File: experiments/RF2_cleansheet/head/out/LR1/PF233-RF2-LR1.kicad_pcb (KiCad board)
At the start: 2 copper layers, 150 x 150 mm, 94 parts

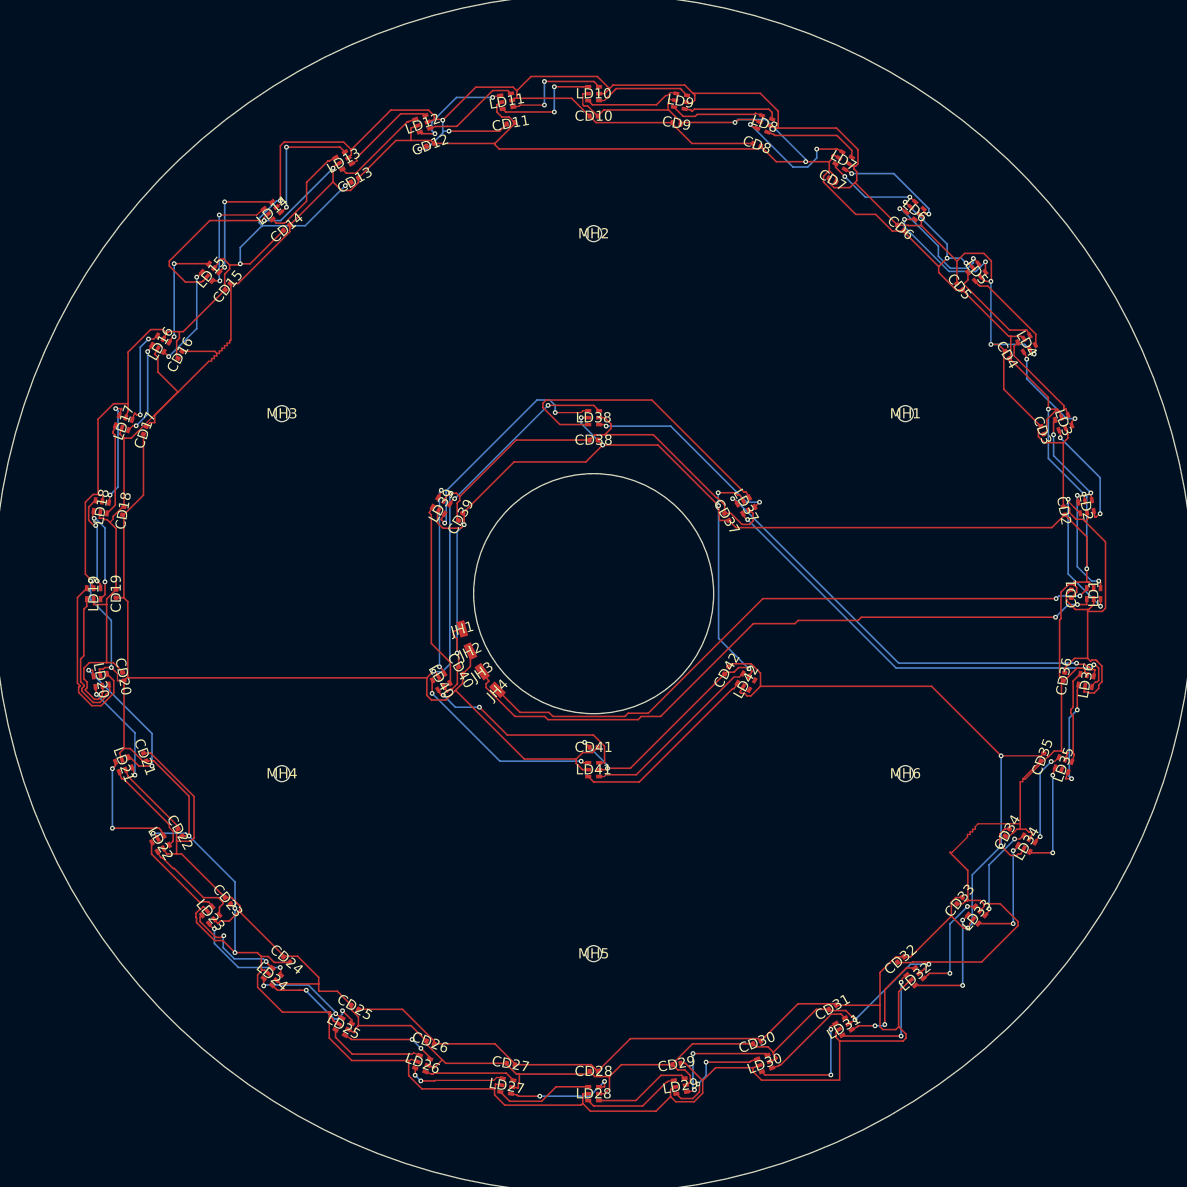
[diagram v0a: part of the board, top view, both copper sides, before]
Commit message: RF2: LED ring LR1 routed by a deterministic template (no autorouter), sign-off PASS
- rf2_ring_template.py: one cell per LED (data outer lane, clock inner lane, never crossing on a layer), chain links, power stubs to the open B.Cu buses, B.Cu crossings under the radial hinge feeds, and the 4 irregular links (hinge feeds, outer-to-inner jump). LR1: KiCad DRC 0, 0 unconnected, min clearance 0.19 mm (rule 0.10), no loop around the axis, parity, Gerbers; builds in 14 s. Freerouting had stalled (no pass in 5 min for 4 connections)
- netlist: LR1 capacitors rotated (+5V pin on the VDD side), hinge lands JH3 = clock / JH4 = data (harness C10c/C10d follow)
- rf2_boards: no autorouter run when nothing is open (template, pre-routes or resumed copper); board-setup via minima and a .kicad_dru written beside each board; freeroute --no-fanout for resumes
- rf2_head: LED envelope no longer empty (zero-height solid), capacitor sites added
- sign-off order: ledger before the housing checks. Head mass corrected 702 -> 745 g (docs/CORRECTIONS.md)
- Freerouting scratch folders untracked

Co-Authored-By: Claude Opus 5.5 <noreply@anthropic.com>
Claude-Session: https://claude.ai/code/session_01FX4DWSYYjMCFGGA6gmha65
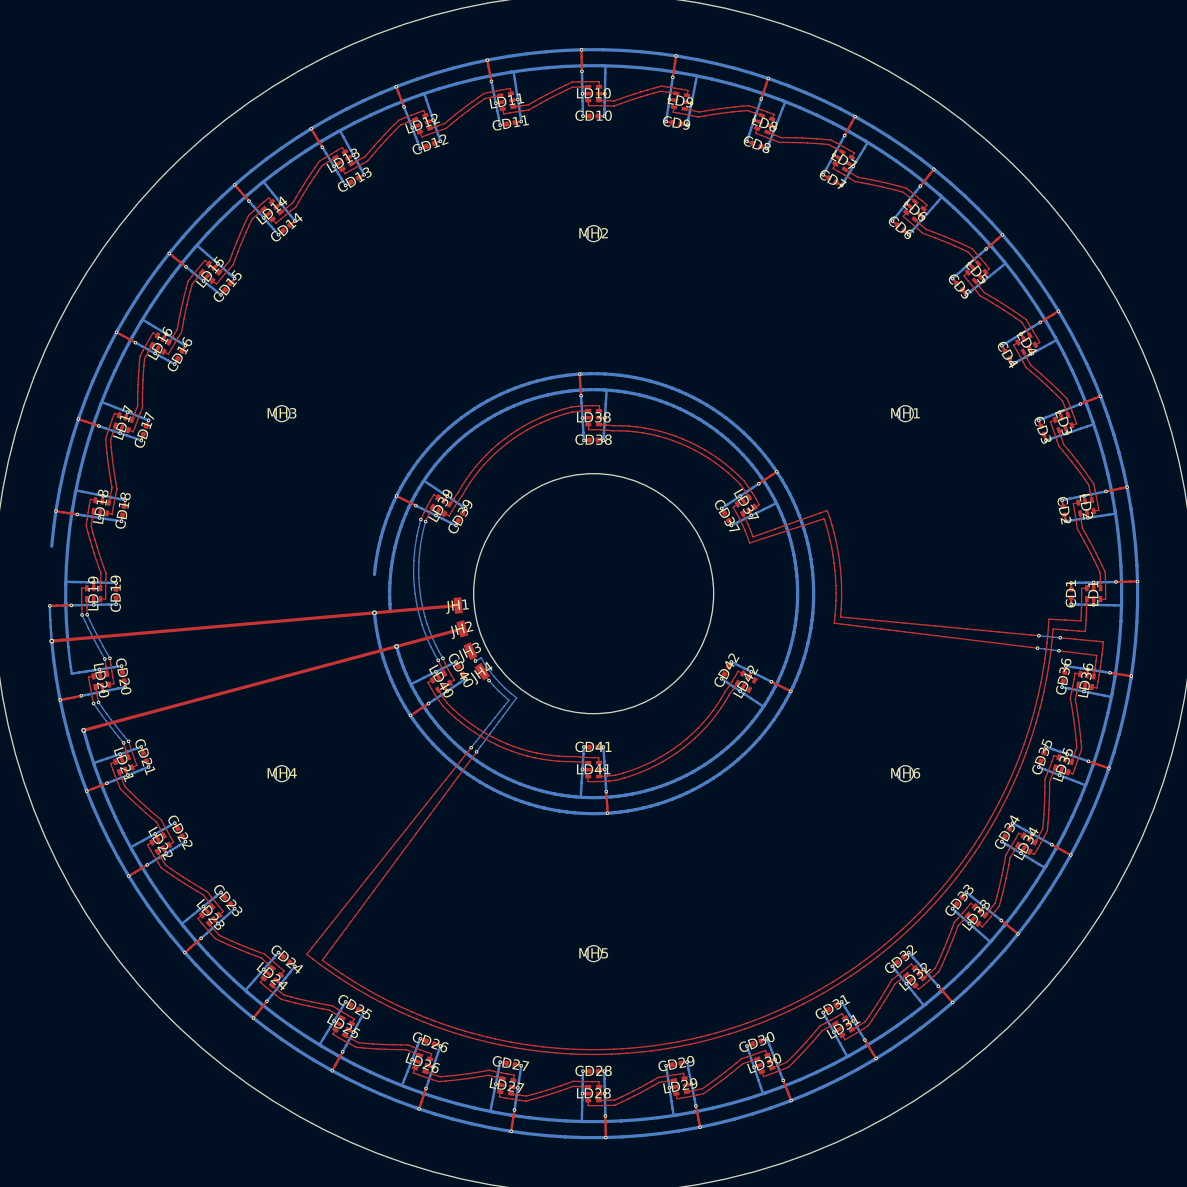
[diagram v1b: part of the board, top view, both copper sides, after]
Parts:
- JH3: value LED_DATA -> LED_CLK
- JH4: value LED_CLK -> LED_DATA
- moved JH2 2.96 mm to (133.6, 154.4), turned to -165 degrees
- moved JH4 2.96 mm to (136.1, 159.8), turned to -145 degrees
- moved JH3 2.96 mm to (134.6, 157.2), turned to -155 degrees
- moved JH1 2.96 mm to (133.1, 151.5), turned to -175 degrees
- turned CD24 to 140 degrees
- turned CD5 to -50 degrees
- turned CD32 to -140 degrees
- turned CD33 to -130 degrees
- turned CD14 to 40 degrees
- turned CD15 to 50 degrees
- turned CD23 to 130 degrees
- turned CD6 to -40 degrees
- turned CD12 to 20 degrees
- turned CD17 to 70 degrees
- turned CD21 to 110 degrees
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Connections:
- JH3 pad 1: LED_D0 -> LED_C0
- JH4 pad 1: LED_C0 -> LED_D0
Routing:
- net +5V_LED: track 829.6 -> 1052.9 mm, vias 21 -> 170
- net LED_C0: track 81.7 -> 181.1 mm
- net LED_D0: track 85.8 -> 178.4 mm
- net LED_C37: track 38.2 -> 23.4 mm
- net GND: track 953.8 -> 942.3 mm, vias 20 -> 86
- net LED_D36: track 55.7 -> 66.0 mm
- net LED_D19: track 22.2 -> 12.1 mm, vias 0 -> 2
- net LED_C36: track 56.0 -> 64.3 mm
- net LED_D20: track 19.9 -> 12.1 mm
- net LED_D1: track 18.3 -> 12.1 mm, vias 2 -> 0
- net LED_C38: track 29.3 -> 23.4 mm, vias 2 -> 0
- net LED_C19: track 17.7 -> 11.9 mm, vias 0 -> 2
- net LED_C7: track 16.5 -> 11.9 mm, vias 2 -> 0
- net LED_D5: track 16.4 -> 12.1 mm, vias 2 -> 0
- net LED_D13: track 16.0 -> 12.1 mm, vias 2 -> 0
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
